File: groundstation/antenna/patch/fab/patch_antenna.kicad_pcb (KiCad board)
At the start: 2 copper layers, 160 x 160 mm, 0 parts

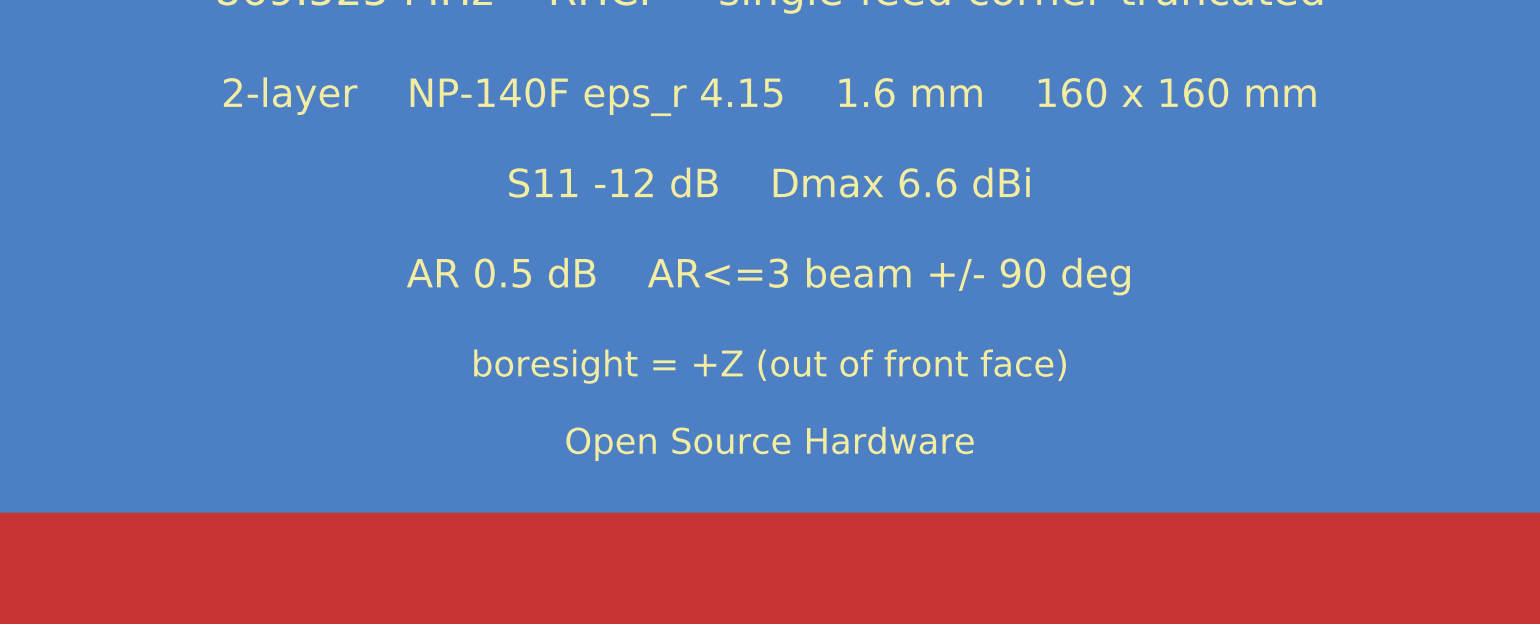
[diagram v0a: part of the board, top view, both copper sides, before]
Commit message: Patch antenna: qualify datasheet AR to band-robust + cone-worst values
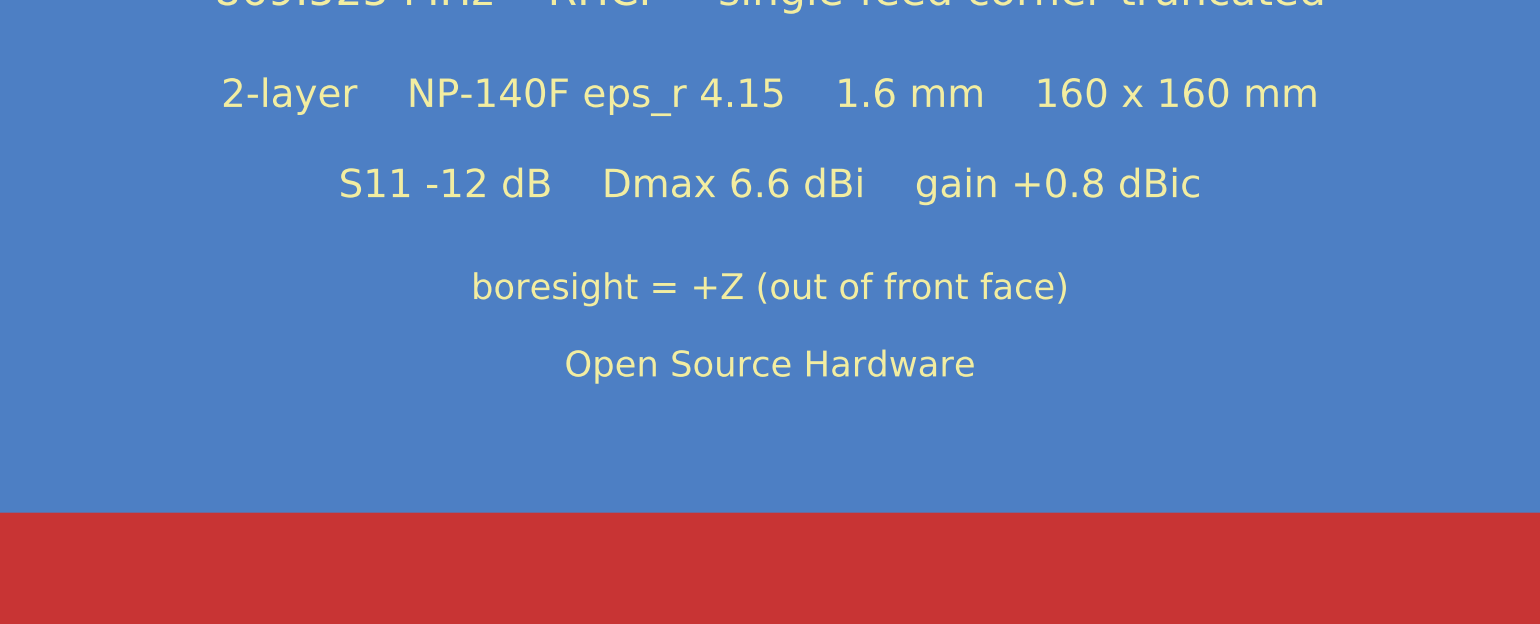
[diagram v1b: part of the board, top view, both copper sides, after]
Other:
- board text added: ">=45 deg cone (worst 1.0 dB)"
- board text added: "AR<=3 coverage"
- board text added: "S11 -12 dB Dmax 6.6 dBi gain +0.8 dBic"
- board text added: "~1.4 dB (band)"
- board text removed: "0.45 dB"
- board text removed: "180 deg"
- board text removed: "AR 0.5 dB AR<=3 beam +/- 90 deg"
- board text removed: "AR<=3 beamwidth"
- board text removed: "S11 -12 dB Dmax 6.6 dBi"
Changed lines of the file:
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@@
     (effects (font (size 1.10 1.10) (thickness 0.154)))
   )
-  (gr_text "S11 -12 dB    Dmax 6.6 dBi"
+  (gr_text "S11 -12 dB    Dmax 6.6 dBi    gain +0.8 dBic"
     (at 80.0000 26.0000) (layer "F.SilkS")
     (effects (font (size 1.10 1.10) (thickness 0.154)))
   )
-  (gr_text "AR 0.5 dB    AR<=3 beam +/- 90 deg"
-    (at 80.0000 29.5000) (layer "F.SilkS")
-    (effects (font (size 1.10 1.10) (thickness 0.154)))
-  )
   (gr_text "boresight = +Z (out of front face)"
+    (at 80.0000 30.0000) (layer "F.SilkS")
+    (effects (font (size 1.00 1.00) (thickness 0.14)))
+  )
+  (gr_text "Open Source Hardware"
     (at 80.0000 33.0000) (layer "F.SilkS")
-    (effects (font (size 1.00 1.00) (thickness 0.14)))
-  )
-  (gr_text "Open Source Hardware"
-    (at 80.0000 36.0000) (layer "F.SilkS")
     (effects (font (size 1.00 1.00) (thickness 0.14)))
   )
@@
     (effects (font (size 1.20 1.20) (thickness 0.168)) (justify mirror left))
   )
-  (gr_text "0.45 dB"
+  (gr_text "~1.4 dB (band)"
     (at 109.2000 74.0960) (layer "B.SilkS")
     (effects (font (size 1.20 1.20) (thickness 0.168)) (justify mirror left))
   )
-  (gr_text "AR<=3 beamwidth"
+  (gr_text "AR<=3 coverage"
     (at 145.2000 79.6960) (layer "B.SilkS")
     (effects (font (size 1.20 1.20) (thickness 0.168)) (justify mirror left))
   )
-  (gr_text "180 deg"
+  (gr_text ">=45 deg cone (worst 1.0 dB)"
     (at 109.2000 79.6960) (layer "B.SilkS")
     (effects (font (size 1.20 1.20) (thickness 0.168)) (justify mirror left))
